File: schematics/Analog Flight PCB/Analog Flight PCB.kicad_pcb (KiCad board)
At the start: 2 copper layers, 94.6 x 50.9 mm, 150 parts, among them J1 20-Pin Interconnect, J10 Conn_01x02_Male, J11 Conn_01x02_Male, J12 Conn_01x02_Male, J13 Conn_01x02_Male, J14 Conn_01x02_Male, J15 Conn_01x02_Male, J16 Conn_01x02_Male, J2 Conn_01x05_Male, J3 Conn_01x05_Male, J4 Conn_01x05_Male, J5 Conn_01x03_Male, J6 Conn_01x03_Male, J7 Conn_01x03_Male, J8 Conn_01x02_Male, J9 Conn_01x02_Male, M1 MountingHole_3.2mm_M3_Pad_Via, M2 MountingHole_3.2mm_M3_Pad_Via, M3 MountingHole_3.2mm_M3_Pad_Via, M4 MountingHole_3.2mm_M3_Pad_Via, Q1 BSS138, Q2 BSS138, Q3 BSS138, U1 LP2985-3.3, U10 MAX31856, U11 MAX31856, U12 MAX31856, U13 MAX31856, U14 MAX31856, U15 MAX31856, U2 PCA9548ARGE, U3 NAU7802SGI, U4 NAU7802SGI, U5 NAU7802SGI, U6 ADS1015IDGS, U7 MAX31856, U8 MAX31856, U9 MAX31856

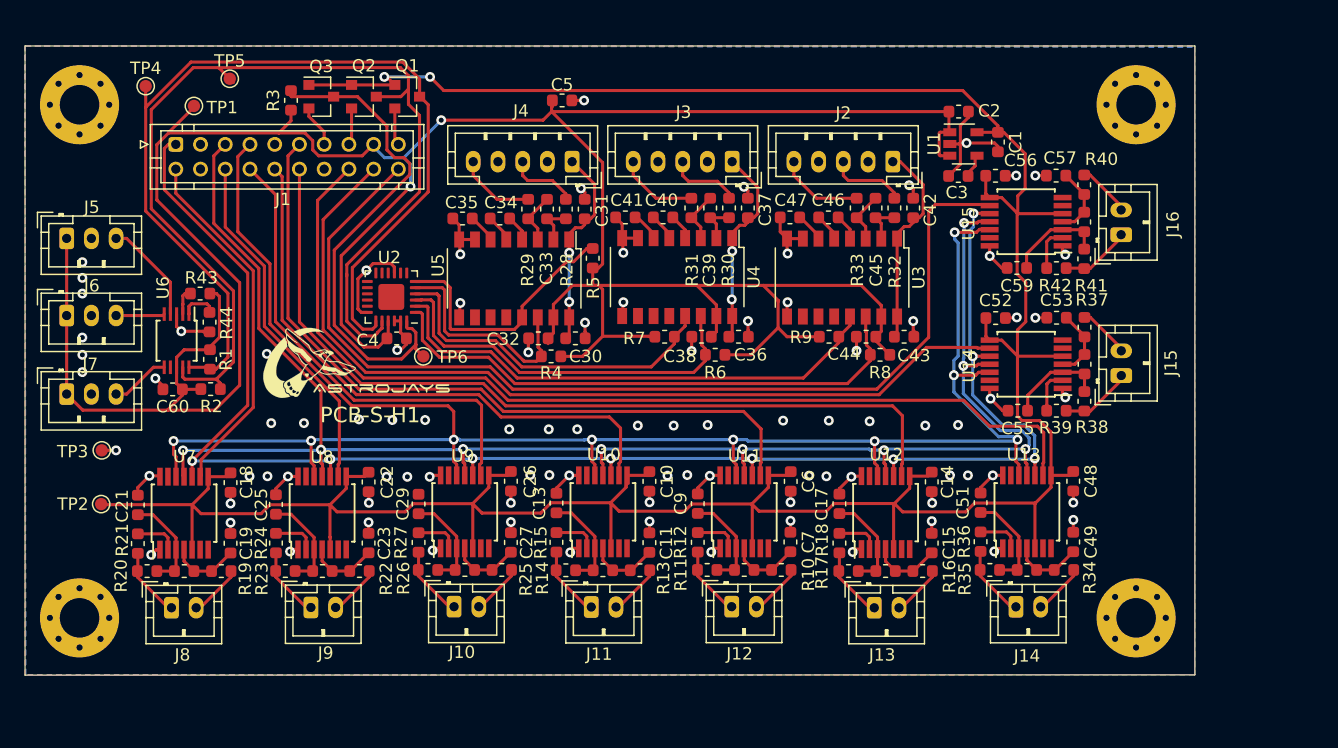
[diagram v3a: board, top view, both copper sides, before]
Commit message: ASPCB: Rev 1.0f
Rerouted with DRDY select lines to I2C GPIO expander. This means that we
can check all of the DRDY lines with one interrupt, so long as we poll
the input expander after recieving each interrupt. This allows us to
switch to interrupt driven programming, which should enhance the data
collection speed while reducing CPU use. To accomodate the extra lines,
we have switched to gridded ground style routing.
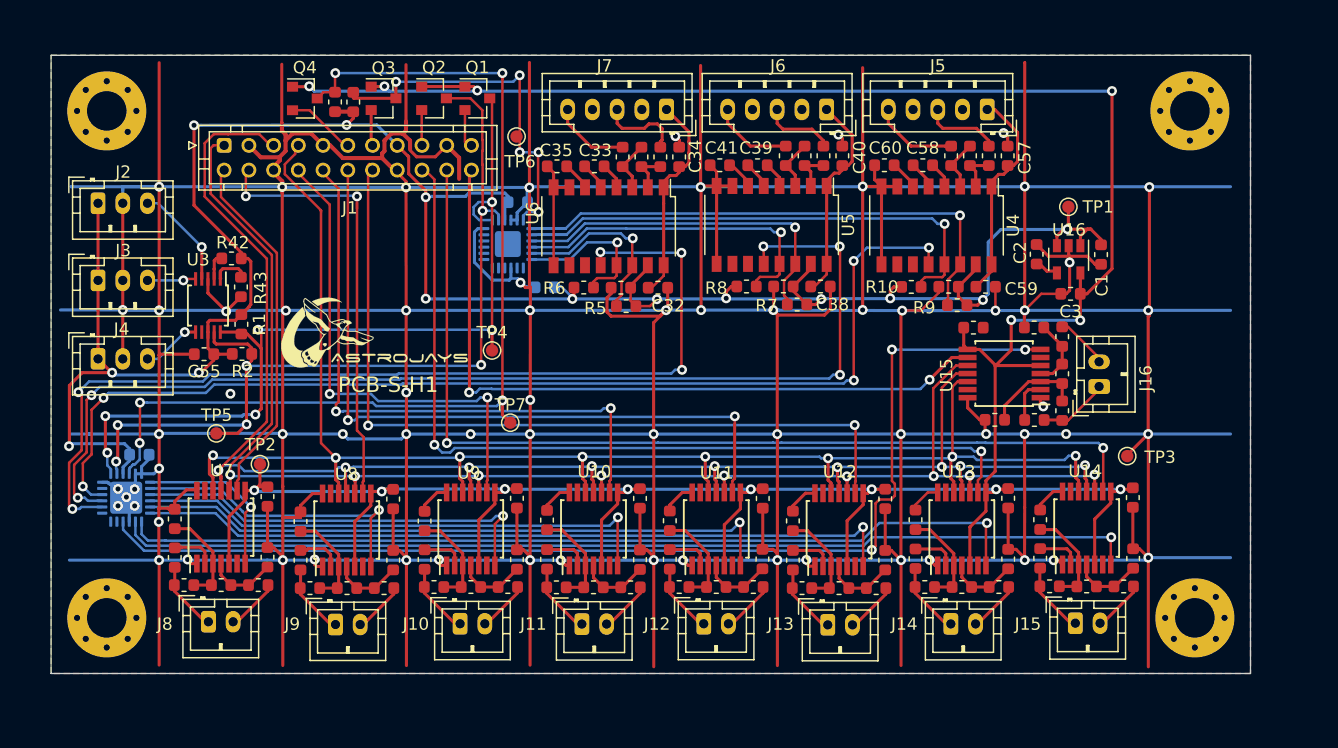
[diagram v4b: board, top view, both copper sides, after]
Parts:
- added C4: 1u, Capacitor_SMD:C_0603_1608Metric, B.Cu at (97.6, 101.8)
- added Q4: BSS138, Package_TO_SOT_SMD:SOT-23, F.Cu at (111.0, 73.0)
- added R4: 10k, Resistor_SMD:R_0603_1608Metric, F.Cu at (113.5, 73.3)
- added TP7: TP_5V_I2C1_RST, TestPoint:TestPoint_Pad_D1.0mm, F.Cu at (127.6, 99.2)
- added U1: TCA9555RTWR, Package_DFN_QFN:QFN-24-1EP_4x4mm_P0.5mm_EP2.6x2.6mm, B.Cu at (96.6, 105.3)
- C5, U2: moved to B.Cu
- C6: renamed from C4; moved to B.Cu
- J1: value 20-Pin Interconnect -> 22 Pin inconnnect; footprint Connector_JST:JST_PHD_B20B-PHDSS_2x10_P2.00mm_Vertical -> Connector_JST:JST_PHD_B22B-PHDSS_2x11_P2.00mm_Vertical
- moved TP3 82.9 mm to (177.5, 101.9)
- moved TP1 71.2 mm to (172.8, 81.8)
- moved M3 41.8 mm to (183.0, 115.0)
- moved M4 41.2 mm to (182.6, 74.0)
- moved TP4 35.2 mm to (126.2, 93.4)
- moved TP5 28.7 mm to (103.9, 100.1)
- moved R36 21.2 mm to (177.2, 112.5), turned to 180 degrees
- moved C47 20.4 mm to (178.0, 110.2), turned to 270 degrees
- moved J15 20.4 mm to (173.3, 115.4), turned to 0 degrees
- moved TP6 19.3 mm to (128.1, 76.1)
- moved C50 18.3 mm to (178.0, 105.3), turned to 270 degrees
- moved C48 18.0 mm to (174.2, 112.5), turned to 180 degrees
- moved C1 16.3 mm to (175.4, 85.6), turned to 270 degrees
- moved R37 15.2 mm to (171.3, 112.4), turned to 180 degrees
- moved C5 15.2 mm to (130.4, 88.3), turned to 180 degrees
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- renumbered C2 to C1, C6 to C10, C10 to C14, C14 to C18, C3 to C2, C18 to C22, C22 to C26, C1 to C3, C26 to C30, C33 to C31, C30 to C32, C34 to C33, C31 to C34, C32 to C36, C39 to C37, C36 to C38, C40 to C39, C37 to C40, C38 to C42, C49 to C43, C50 to C44, C51 to C45, C48 to C46, C53 to C47, C54 to C48, C55 to C49, C52 to C50, C57 to C51, C58 to C52, C59 to C53, C56 to C54, C60 to C55, C45 to C56, C42 to C57, C46 to C58, C43 to C59, C47 to C60, C44 to C61, J5 to J2, J6 to J3, J7 to J4, J2 to J5, J3 to J6, J4 to J7, R9 to R10, R10 to R11, R11 to R12, R12 to R13, R13 to R14, R14 to R15, R15 to R16, R16 to R17, R17 to R18, R18 to R19, R19 to R20, R20 to R21, R21 to R22, R22 to R23, R23 to R24, R24 to R25, R25 to R26, R26 to R27, R27 to R28, R28 to R29, R29 to R30, R30 to R31, R31 to R32, R34 to R33, R35 to R34, R36 to R35, R37 to R36, R38 to R37, R39 to R38, R40 to R39, R41 to R40, R42 to R41, R43 to R42, R44 to R43, R32 to R44, R33 to R45, R4 to R5, R5 to R6, R6 to R7, R7 to R8, R8 to R9, U1 to U16, U6 to U3, U3 to U4, U4 to U5, U5 to U6
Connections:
- net /3V3_I2C1_RESET renamed /3V3_I2C1_RST
- J1 pad 11: /SPI1_CS5 -> /3V3_I2C1_INT
- J1 pad 12: /SPI1_CS6 -> /SPI1_CS5
- J1 pad 14: GND -> /SPI1_CS6
- J1 pad 15: /3V3_I2C1_SDA -> +5V
- J1 pad 16: /SPI1_CS7 -> GND
- J1 pad 17: +5V -> /3V3_I2C1_SDA
- J1 pad 18: /SPI1_CS8 -> /SPI1_CS7
- J1 pad 19: /3V3_I2C1_SCL -> GND
- J1 pad 20: /SPI1_CS9 -> /SPI1_CS8
- J1 pad 4: GND -> /SPI1_CS2
- J1 pad 6: /SPI1_CS2 -> GND
- U10 pad 7: Net-(U10-Pad7) -> /SPI1_DRDY4
- U11 pad 7: Net-(U11-Pad7) -> /SPI1_DRDY5
- U12 pad 7: Net-(U12-Pad7) -> /SPI1_DRDY6
- U13 pad 7: Net-(U13-Pad7) -> /SPI1_DRDY7
- U14 pad 7: Net-(U14-Pad7) -> /SPI1_DRDY8
- U15 pad 7: Net-(U15-Pad7) -> /SPI1_DRDY9
- U4 pad 12: /LC1/DRDY -> /LC1_DRDY
- U5 pad 12: /LC2/DRDY -> /LC2_DRDY
- U6 pad 12: /LC3/DRDY -> /LC3_DRDY
- U7 pad 7: Net-(U7-Pad7) -> /SPI1_DRDY1
- U8 pad 7: Net-(U8-Pad7) -> /SPI1_DRDY2
- U9 pad 7: Net-(U9-Pad7) -> /SPI1_DRDY3
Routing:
- net GND: track 102.4 -> 996.3 mm, vias 93 -> 68
- net /SPI1_DRDY9: track 0.00 -> 91.4 mm, vias 0 -> 3
- net /LC2_DRDY: track 0.00 -> 90.5 mm, vias 0 -> 5
- net /LC1_DRDY: track 0.00 -> 88.5 mm, vias 0 -> 5
- net /SPI1_DRDY8: track 0.00 -> 82.9 mm, vias 0 -> 1
- net /5V_I2C1_INT: track 0.00 -> 81.5 mm, vias 0 -> 5
- net /LC3_DRDY: track 0.00 -> 79.2 mm, vias 0 -> 5
- net /SPI1_DRDY7: track 0.00 -> 73.7 mm, vias 0 -> 1
- net /SPI1_DRDY6: track 0.00 -> 61.9 mm, vias 0 -> 1
- net +5V: track 251.6 -> 197.4 mm, vias 2 -> 14
- net /SPI1_DRDY5: track 0.00 -> 52.3 mm, vias 0 -> 1
- net /SPI1_DRDY4: track 0.00 -> 42.8 mm, vias 0 -> 1
- net /SPI1_DRDY3: track 0.00 -> 33.9 mm, vias 0 -> 1
- net /SPI1_DRDY2: track 0.00 -> 24.5 mm, vias 0 -> 1
- net /SPI1_CS9: track 82.9 -> 59.7 mm, vias 0 -> 2
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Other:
- board size 94.6 x 50.9 mm -> 97 x 50 mm
- net class Default: trace_width 0.25 -> 0.2032
- net class Power added: clearance 0.2, trace_width 0.25, via_dia 0.8, via_drill 0.4
- board text added: "DAQ Sensors PCB - Rev 1.0f Part ID: PCB-S-H1 Astrojays Rocketry JHU, Jan 2020"
- board text removed: "DAQ Sensors PCB - Rev 1.0e Part ID: PCB-S-H1 Astrojays Rocketry JHU, Jan 2020"

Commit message: ASPCB: Rev 1.0g
Final revision in the 1.0 series, adding power-on indicator and low pass
filtering for ADC @ 1.59kHz to prevent aliasing. This revision is ready
for fab and prototyping. Obsolete PCA9548A has been replaced by current
part TCA9548A.
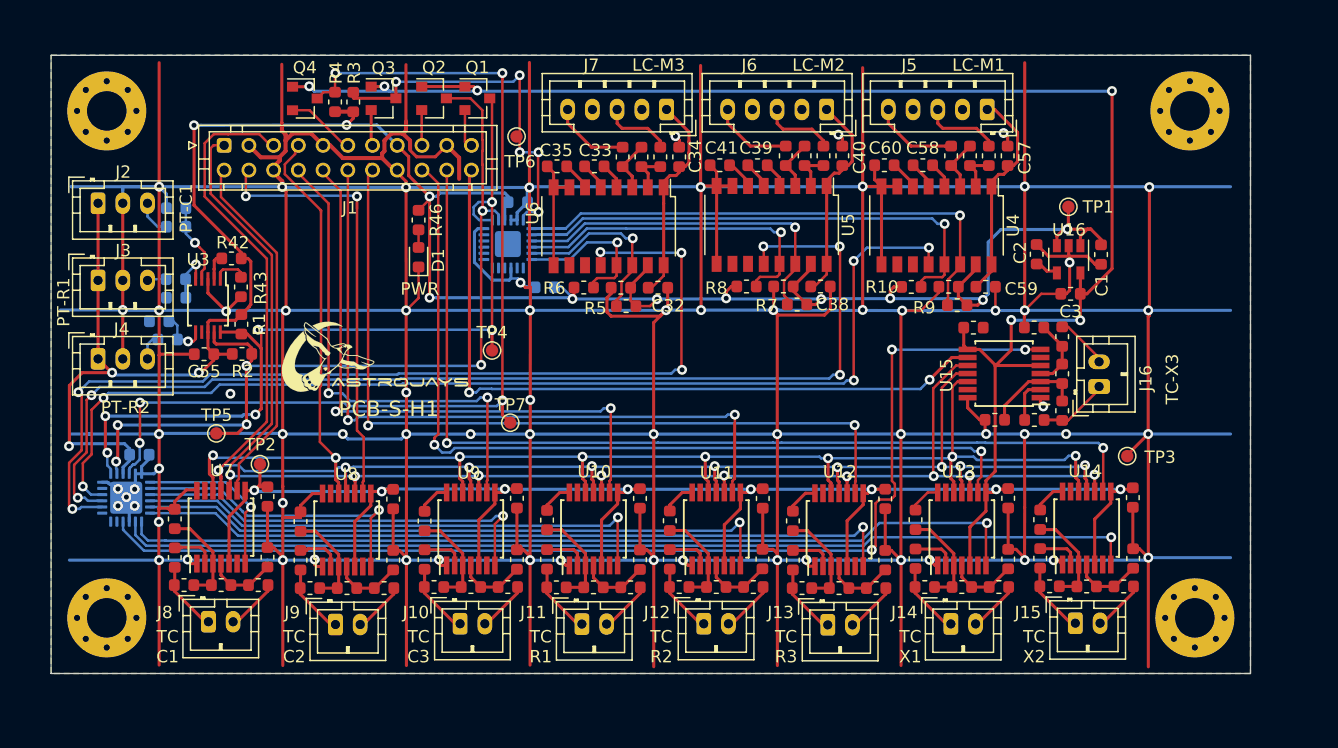
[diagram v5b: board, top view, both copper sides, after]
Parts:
- added C62: 0.1u, Capacitor_SMD:C_0603_1608Metric, B.Cu at (100.6, 81.9)
- added C63: 0.1u, Capacitor_SMD:C_0603_1608Metric, B.Cu at (100.6, 89.1)
- added C64: 0.1u, Capacitor_SMD:C_0603_1608Metric, B.Cu at (99.2, 91.0)
- added D1: LED, LED_SMD:LED_0603_1608Metric, F.Cu at (120.2, 85.8)
- added R46: 1k, Resistor_SMD:R_0603_1608Metric, F.Cu at (120.2, 82.8)
- added R47: 1k, Resistor_SMD:R_0603_1608Metric, B.Cu at (100.6, 83.4)
- added R48: 1k, Resistor_SMD:R_0603_1608Metric, B.Cu at (100.6, 87.6)
- added R49: 1k, Resistor_SMD:R_0603_1608Metric, B.Cu at (99.9, 92.5)
- R1, R10, R2, R5, R6, R7, R8, R9: value 10k -> 2k2
- R3, R4: value 10k -> 4k7
- TP7: value TP_5V_I2C1_RST -> TP_5V_I2C1_INT
- U2: value PCA9548ARGE -> TCA9548ARGER
- moved G*** 5.87 mm to (154.5, 109.5)
- moved G*** 1.96 mm to (118.3, 93.6)
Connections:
- U3 pad 4: Net-(J2-Pad3) -> Net-(C62-Pad1)
- U3 pad 5: Net-(J3-Pad3) -> Net-(C63-Pad1)
- U3 pad 6: Net-(J4-Pad3) -> Net-(C64-Pad1)
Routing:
- net Net-(C62-Pad1): track 0.00 -> 6.44 mm, vias 0 -> 1
- net Net-(J2-Pad3): track 8.44 -> 2.94 mm, vias 1 -> 0
- net GND: track 996.3 -> 1001.2 mm, vias 68 -> 69
- net Net-(C63-Pad1): track 0.00 -> 4.23 mm, vias 0 -> 1
- net Net-(C64-Pad1): track 0.00 -> 4.15 mm, vias 0 -> 1
- net Net-(J4-Pad3): track 4.79 -> 2.17 mm, vias 1 -> 0
- net Net-(J3-Pad3): track 4.11 -> 1.57 mm, vias 1 -> 0
- net Net-(D1-Pad2): track 0.00 -> 1.43 mm
- net Net-(J7-Pad3): track 6.80 -> 5.72 mm
- net +5V: track 197.4 -> 198.3 mm
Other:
- board text added: "DAQ Sensors PCB - Rev 1.0g Part ID: PCB-S-H1 Astrojays Rocketry JHU, Feb 2020"
- board text added: "LC-M1"
- board text added: "LC-M2"
- board text added: "LC-M3"
- board text added: "PT-C1"
- board text added: "PT-R1"
- board text added: "PT-R2"
- board text added: "PWR"
- board text added: "TC C1"
- board text added: "TC C2"
- board text added: "TC C3"
- board text added: "TC R1"
- board text added: "TC R2"
- board text added: "TC R3"
- board text added: "TC X1"
- board text added: "TC X2"
- board text added: "TC-X3"
- board text removed: "DAQ Sensors PCB - Rev 1.0f Part ID: PCB-S-H1 Astrojays Rocketry JHU, Jan 2020"
